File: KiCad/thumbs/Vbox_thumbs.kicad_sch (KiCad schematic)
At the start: 4 parts, among them J1 Conn_01x06, J2 Conn_01x06, J6 Conn_01x10, J7 Conn_01x10

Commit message: thumbs and fingers
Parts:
- removed J6, J7: Conn_01x10, Connector_JST:JST_PH_S10B-PH-SM4-TB_1x10-1MP_P2.00mm_Horizontal, symbol Connector_Generic:Conn_01x10
- added SW1, SW10, SW2, SW3, SW4, SW5, SW6, SW7, SW8, SW9: SW_Push_45deg, Buttons:Vbox, symbol Switch:SW_Push_45deg
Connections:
- net A: now also SW6.1
- net C_DN: now also SW10.1
- net C_LT: now also SW9.1
- net C_RT: now also SW7.1
- net C_UP: now also SW8.1
- net GND: now also SW1.2, SW10.2, SW2.2, SW3.2, SW4.2, SW5.2, SW6.2, SW7.2, SW8.2, SW9.2
- net M1: now also SW1.1
- net M2: now also SW5.1
- net M3: now also SW4.1
- net M4: now also SW3.1
- net M5: now also SW2.1

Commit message: fix drc errors
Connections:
- net A: now also J2.3 (Pin_3); no longer J2.4 (Pin_4)
- net C_DN: now also J2.2 (Pin_2); no longer J2.5 (Pin_5)
- net C_LT: now also J2.4 (Pin_4); no longer J2.3 (Pin_3)
- net C_RT: now also J2.1 (Pin_1); no longer J2.6 (Pin_6)
- net C_UP: now also J2.5 (Pin_5); no longer J2.2 (Pin_2)
- net GND: now also J2.6 (Pin_6); no longer J2.1 (Pin_1)

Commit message: make both sides share holes
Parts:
- SW10, SW6, SW7, SW8, SW9: footprint Buttons:Vbox -> Buttons:Vbox_1
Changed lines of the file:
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@@
       (effects (font (size 1.27 1.27)))
     )
-    (property "Footprint" "Buttons:Vbox" (at 195.58 68.58 0)
+    (property "Footprint" "Buttons:Vbox_1" (at 195.58 68.58 0)
       (effects (font (size 1.27 1.27)) hide)
     )
@@
       (effects (font (size 1.27 1.27)))
     )
-    (property "Footprint" "Buttons:Vbox" (at 237.49 66.04 0)
+    (property "Footprint" "Buttons:Vbox_1" (at 237.49 66.04 0)
       (effects (font (size 1.27 1.27)) hide)
     )
@@
       (effects (font (size 1.27 1.27)))
     )
-    (property "Footprint" "Buttons:Vbox" (at 215.9 58.42 0)
+    (property "Footprint" "Buttons:Vbox_1" (at 215.9 58.42 0)
       (effects (font (size 1.27 1.27)) hide)
     )
@@
       (effects (font (size 1.27 1.27)) hide)
     )
+    (property "Field4" "" (at 215.9 58.42 0)
+      (effects (font (size 1.27 1.27)) hide)
+    )
     (pin "1")
     (pin "2")
@@
       (effects (font (size 1.27 1.27)))
     )
-    (property "Footprint" "Buttons:Vbox" (at 194.31 96.52 0)
+    (property "Footprint" "Buttons:Vbox_1" (at 194.31 96.52 0)
       (effects (font (size 1.27 1.27)) hide)
     )
@@
       (effects (font (size 1.27 1.27)))
     )
-    (property "Footprint" "Buttons:Vbox" (at 217.17 82.55 0)
-      (effects (font (size 1.27 1.27)) hide)
-    )
+    (property "Footprint" "Buttons:Vbox_1" (at 217.17 82.55 0)
+      (effects (font (size 1.27 1.27)) hide)
+    )

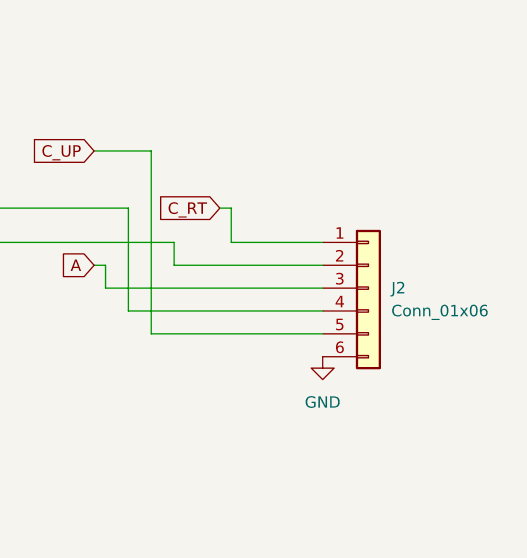
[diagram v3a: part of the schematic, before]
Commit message: flip connectors
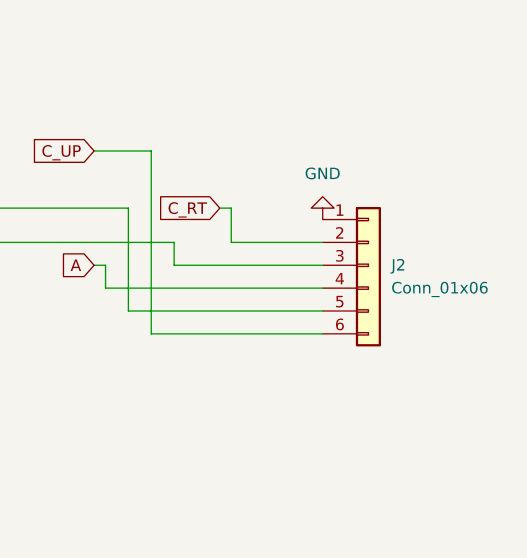
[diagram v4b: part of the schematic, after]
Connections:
- net A: now also J2.4 (Pin_4); no longer J2.3 (Pin_3)
- net C_DN: now also J2.3 (Pin_3); no longer J2.2 (Pin_2)
- net C_LT: now also J2.5 (Pin_5); no longer J2.4 (Pin_4)
- net C_RT: now also J2.2 (Pin_2); no longer J2.1 (Pin_1)
- net C_UP: now also J2.6 (Pin_6); no longer J2.5 (Pin_5)
- net GND: now also J2.1 (Pin_1); no longer J2.6 (Pin_6)
